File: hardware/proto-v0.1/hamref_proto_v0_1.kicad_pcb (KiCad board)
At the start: 4 copper layers, 100 x 100 mm, 113 parts, among them J1 5V_EXT, J10 J RUN (short=MCU reset), J11 J SPARE GPIO, J2 SMA ANT, J3 BNC REF OUT, J4 BNC 1PPS OUT, J5 BNC AUX OUT, J6 J OLED 0.91in I2C, J7 J ENCODER, J8 J LEDS (2x WS2812B), J9 J RESET GNSS (short=reset), U1 TPS2065C, U10 74AHCT1G125, U2 LP5907-3.3, U3 LEA-M8S-0, U4 74LVC1G17, U5 AD5693R, U6 74LVC1G17, U7 74AHCT1G125, U8 74LVC1G125, U9 Si5351C-B-GM, X1 OSC5A2B02, Y1 25MHz

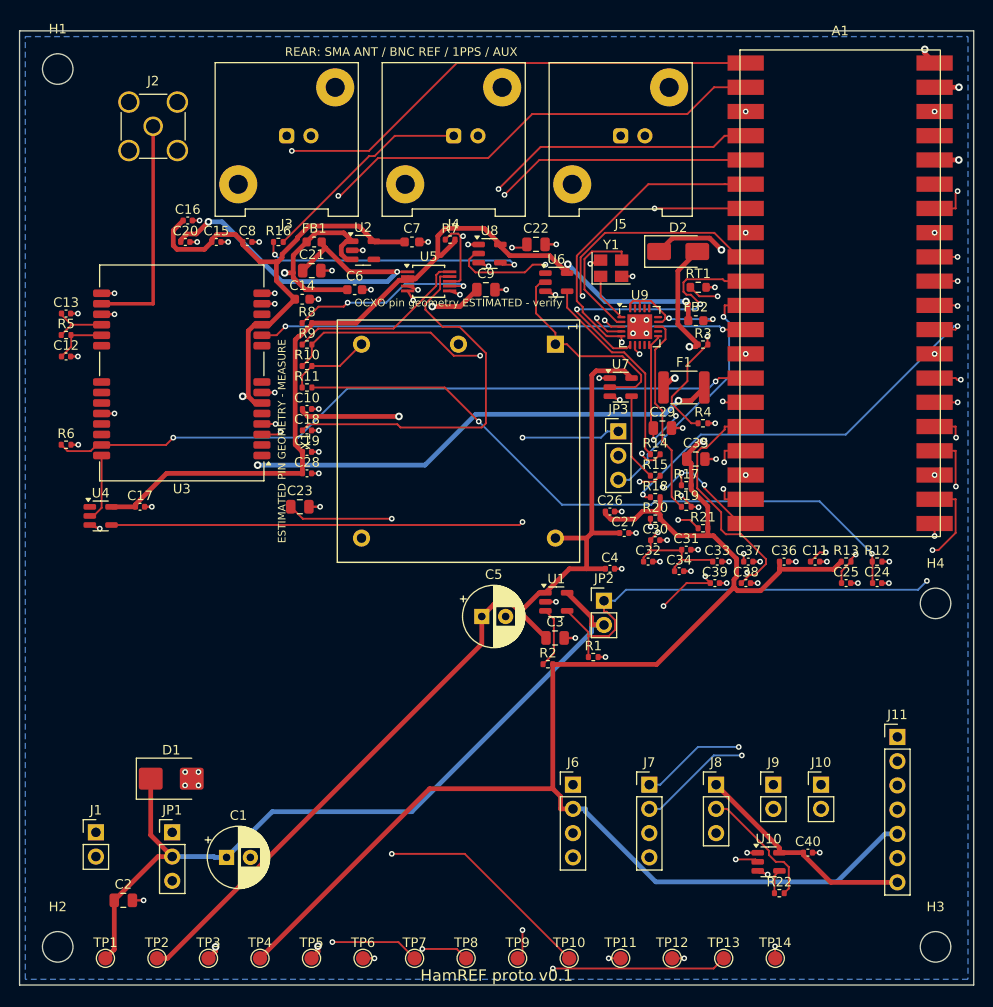
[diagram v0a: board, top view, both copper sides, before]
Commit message: Proto-PCB v0.1: logo, silk cleanup, 3D model paths
- Vectorised HamREF by OH2LAK logo + satellite from the enclosure mockup (make_logo.py)
- silk_pass.py: place reference designators after routing, avoiding pads/vias/outlines
- Fix 3D model paths for KiCad 10 (${KICAD10_3DMODEL_DIR}, .step); box models for OCXO and RP2350-Plus
- route.sh: resume Freerouting from previous partial result; run silk pass before DRC
- DRC: 0 unconnected, 0 clearance, no silk overlaps

Co-Authored-By: Claude Sonnet 5.5 <noreply@anthropic.com>
Claude-Session: https://claude.ai/code/session_01BBEBh5Nhxyv6s49uSZkpLo
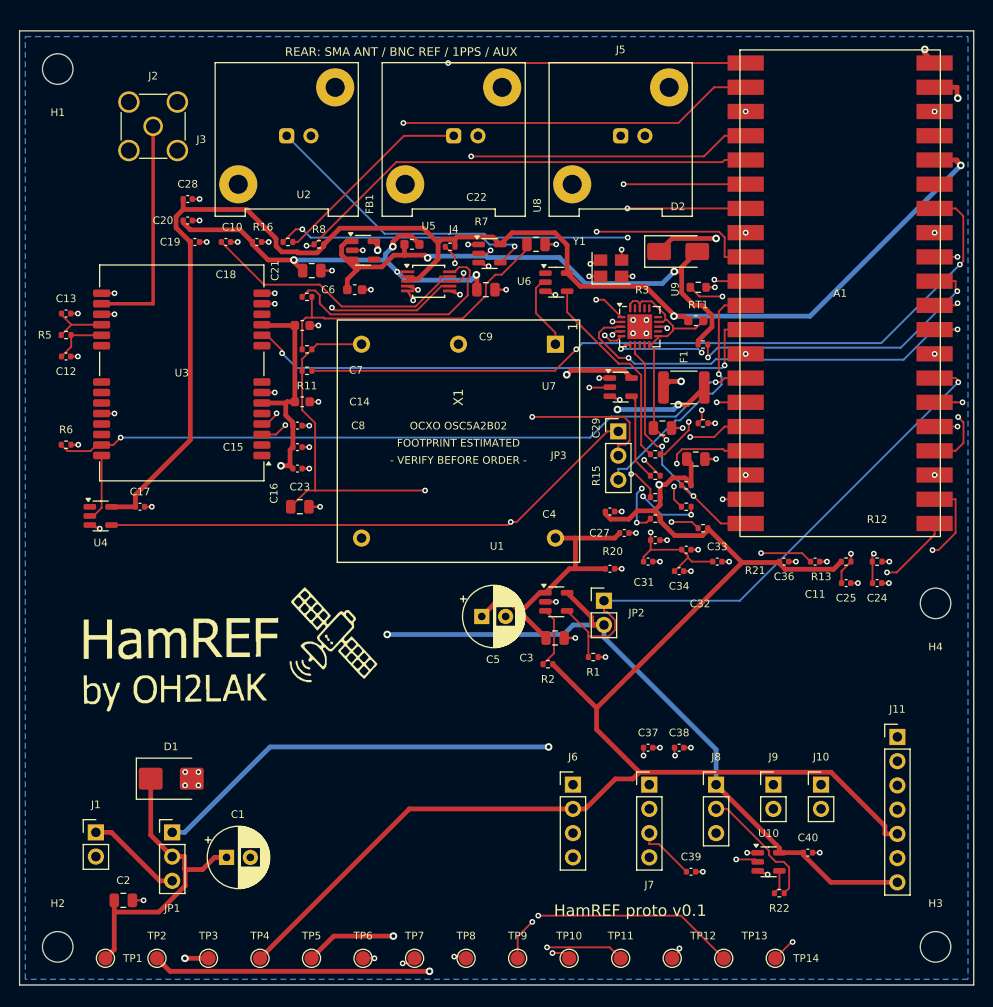
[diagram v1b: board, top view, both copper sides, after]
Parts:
- moved C28 31.3 mm to (67.6, 57.6)
- moved C39 30.4 mm to (120.4, 128.1)
- moved C16 28.4 mm to (79.1, 85.9)
- moved C19 24.9 mm to (68.4, 62.1)
- moved C15 23.1 mm to (79.1, 83.6)
- moved C37 22.1 mm to (115.9, 115.1)
- moved C18 21.5 mm to (71.6, 62.1)
- moved C8 20.0 mm to (79.1, 81.4)
- moved C38 18.6 mm to (119.1, 115.1)
- moved C10 18.3 mm to (74.9, 62.1)
- moved C7 14.5 mm to (79.6, 70.9)
- moved C14 10.8 mm to (79.6, 78.9)
- moved FB1 10.3 mm to (91.1, 62.4)
- moved R8 8.34 mm to (81.4, 62.4)
- moved R9 5.00 mm to (80.1, 67.9)
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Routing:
- net OCXO_10M_3V3: track 63.1 -> 34.1 mm, vias 3 -> 4
- net 5V_MAIN: track 262.7 -> 239.4 mm, vias 2 -> 3
- net 5V_OCXO: track 101.5 -> 123.2 mm, vias 0 -> 2
- net ADC_5V: track 86.3 -> 66.0 mm, vias 3 -> 4
- net ADC_NTC: track 79.9 -> 61.8 mm
- net GNSS_RXD: track 156.5 -> 174.2 mm
- net GNSS_TXD: track 144.5 -> 159.8 mm
- net I2C0_SDA: track 95.1 -> 110.2 mm, vias 2 -> 4
- net 3V3: track 309.0 -> 321.9 mm, vias 4 -> 3
- net 5V_DAC: track 135.9 -> 123.0 mm
- net I2C1_SCL: track 58.3 -> 70.8 mm, vias 3 -> 2
- net 3V3_SYN: track 61.3 -> 48.9 mm, vias 5 -> 2
- net DAC_VREF: track 40.5 -> 28.4 mm
- net PPS_GNSS: track 157.4 -> 146.1 mm, vias 4 -> 3
- net OCXO_EN: track 72.6 -> 61.9 mm, vias 2 -> 1
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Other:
- board text added: "- VERIFY BEFORE ORDER -"
- board text added: "FOOTPRINT ESTIMATED"
- board text added: "OCXO OSC5A2B02"
- board text removed: "OCXO pin geometry ESTIMATED - verify"

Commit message: Proto-PCB v0.1: silk labels for connectors, jumpers and test points
- silk_pass.py adds function and pin-name labels (J1, J6-J11, JP1-3), rear-panel names, TP net names
- Reference designators avoid tracks where possible
- Proto text moved under the logo

Co-Authored-By: Claude Sonnet 5.5 <noreply@anthropic.com>
Claude-Session: https://claude.ai/code/session_01BBEBh5Nhxyv6s49uSZkpLo
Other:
- board text added: "+5V"
- board text added: "1PPS"
- board text added: "3V3"
- board text added: "3V3_GN"
- board text added: "5V"
- board text added: "5V_DAC"
- board text added: "5V_OX"
- board text added: "A"
- board text added: "AUX"
- board text added: "B"
- board text added: "DIN"
- board text added: "EFC"
- board text added: "EN"
- board text added: "EN=short: OCXO always on"
- board text added: "ENCODER"
- board text added: "EXT 5V"
- board text added: "FLT"
- board text added: "GND"
- board text added: "GNSS ANT"
- board text added: "GNSS RST"
- board text added: "GP17"
- board text added: "GP18"
- board text added: "GP19"
- board text added: "GP20"
- board text added: "GRXD"
- board text added: "GTXD"
- board text added: "JP3 1PPS SRC 1-2 GNSS 2-3 MCU"
- board text added: "LEDS"
- board text added: "MCU RST"
- board text added: "OCXO"
- board text added: "OCXO ON"
- board text added: "OLED"
- board text added: "PPS"
- board text added: "PPS_G"
- board text added: "PWR SEL 1-2 USB 2-3 EXT"
- board text added: "REF 10M"
- board text added: "RUN"
- board text added: "SCL"
- board text added: "SDA"
- board text added: "SPARE"
- board text added: "SW"
- board text removed: "REAR: SMA ANT / BNC REF / 1PPS / AUX"

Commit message: Proto-PCB v0.1: GND pours on all copper planes, edge via fence, stitching vias
- F.Cu GND pour was missing (rule areas suppressed it in import_ses.py): fixed
- gnd_finish.py: thermal-relief pours, RF no-pour strip along GNSS_RF, edge via fence, 6 mm stitching grid
- route.sh: silk_pass then gnd_finish before DRC

Co-Authored-By: Claude Sonnet 5.5 <noreply@anthropic.com>
Claude-Session: https://claude.ai/code/session_01BBEBh5Nhxyv6s49uSZkpLo
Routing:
- net GND: vias 81 -> 259
- added copper zone on F.Cu, net GND

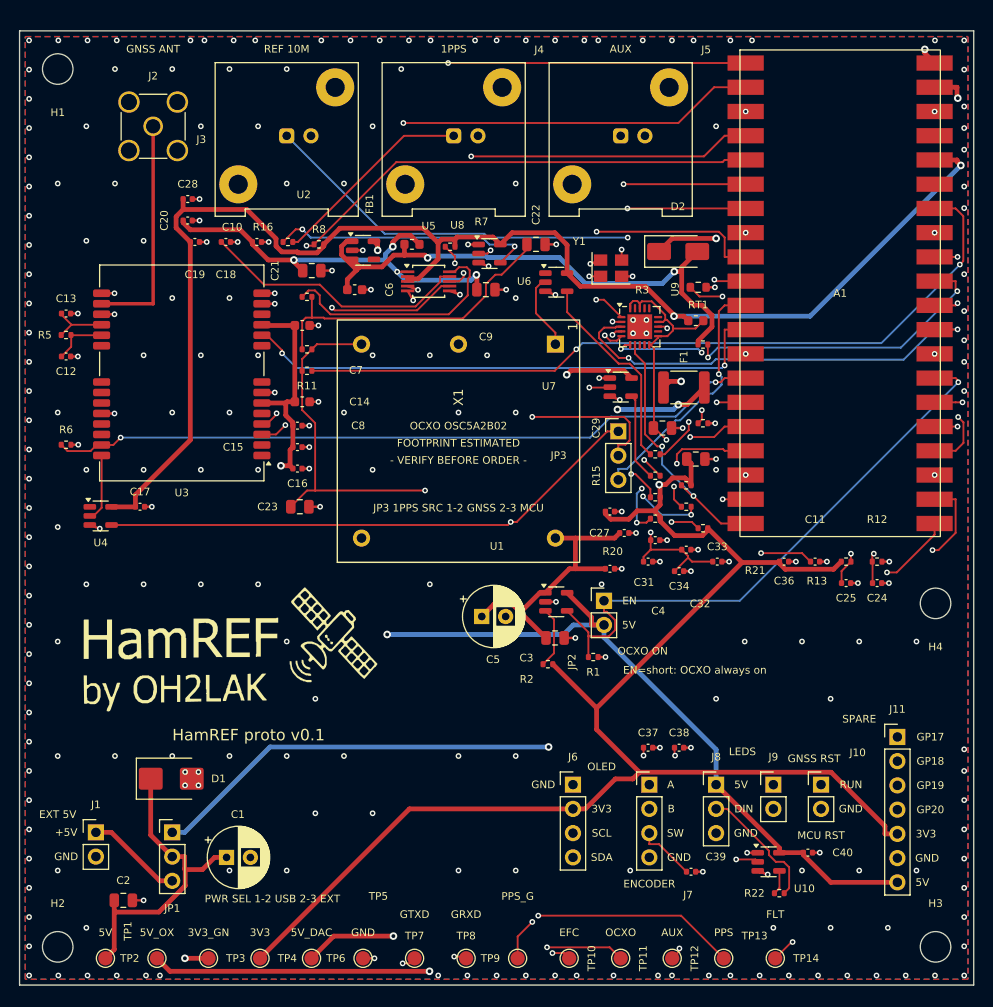
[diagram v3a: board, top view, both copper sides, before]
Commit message: Proto-PCB v0.1: fit Fischer AKG 105.26 case (100x80 mm)
Board 100x100 -> 100x80 mm, R1.5 mm corners, no mounting holes (slides into
case grooves), unmasked GND copper strips along both long edges, horizontal
BNC/SMA connectors for the 15.2 mm height budget, router/test-point fixes.
Docs updated to v0.18.

Co-Authored-By: Claude Sonnet 5.5 <noreply@anthropic.com>
Claude-Session: https://claude.ai/code/session_01BBEBh5Nhxyv6s49uSZkpLo
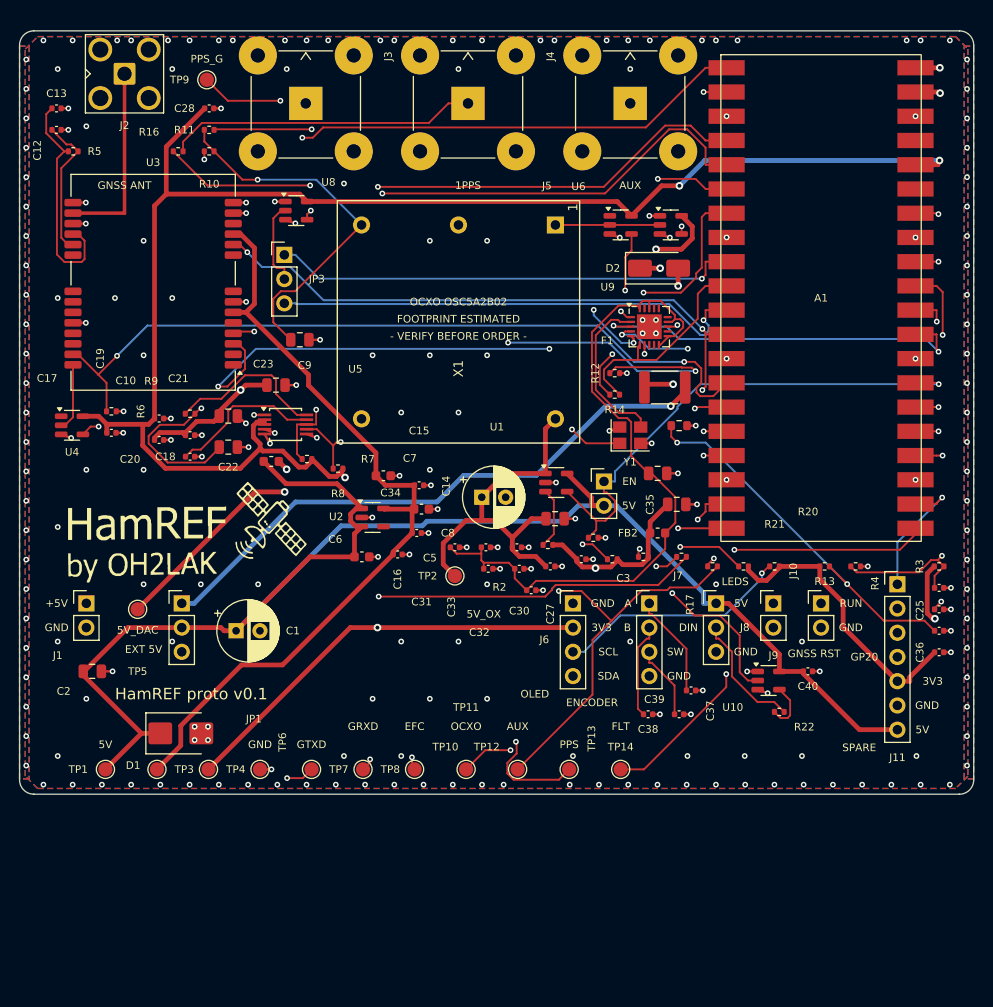
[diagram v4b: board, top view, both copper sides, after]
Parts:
- removed H1, H2, H3, H4: MountingHole_M3, MountingHole_3.2mm_M3
- J2: footprint SMA_Amphenol_901-144_Vertical -> SMA_Amphenol_901-143_Horizontal
- J3, J4, J5: footprint BNC_Amphenol_031-5539_Vertical -> BNC_TEConnectivity_1478035_Horizontal
- moved TP9 97.7 mm to (69.6, 45.1)
- moved TP2 50.8 mm to (95.6, 97.1)
- moved TP5 40.9 mm to (62.4, 100.6)
- moved JP3 39.6 mm to (77.8, 63.5)
- moved C22 38.6 mm to (71.9, 83.6)
- moved R3 34.0 mm to (146.4, 96.1)
- moved R12 33.9 mm to (112.4, 75.9)
- moved U2 28.0 mm to (87.0, 91.0)
- moved C6 28.0 mm to (85.9, 95.1)
- moved R11 27.3 mm to (69.9, 50.4)
- moved FB1 27.1 mm to (76.4, 85.1)
- moved R7 26.8 mm to (80.1, 84.9)
- moved TP11 25.6 mm to (96.8, 117.4)
- moved TP12 25.6 mm to (102.2, 117.4)
- moved TP13 25.6 mm to (107.6, 117.4)
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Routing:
- net 5V_DAC: track 123.0 -> 50.5 mm, vias 5 -> 4
- net 5V_OCXO: track 123.2 -> 68.3 mm, vias 2 -> 1
- net GNSS_RXD: track 174.2 -> 124.3 mm
- net PPS_GNSS: track 146.1 -> 108.4 mm
- net REF_BUF: track 9.16 -> 46.8 mm, vias 0 -> 2
- net GNSS_TXD: track 159.8 -> 126.4 mm, vias 3 -> 4
- net ADC_EFC: track 118.3 -> 150.7 mm, vias 3 -> 5
- net 5V_MAIN: track 239.4 -> 209.0 mm, vias 3 -> 2
- net 5V_USB: track 91.6 -> 62.4 mm, vias 3 -> 1
- net 3V3_GNSS: track 111.9 -> 85.1 mm, vias 3 -> 0
- net PPS_SEL: track 35.5 -> 8.91 mm, vias 2 -> 0
- net I2C1_SDA: track 47.3 -> 73.5 mm, vias 3 -> 2
- net 3V3_SYN: track 48.9 -> 74.2 mm, vias 2 -> 0
- net PPS_MCU: track 26.5 -> 50.7 mm
- net ENC_SW: track 56.2 -> 33.6 mm
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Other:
- board size 100 x 100 mm -> 100 x 80 mm
- board text removed: "3V3_GN"
- board text removed: "EN=short: OCXO always on"
- board text removed: "GP17"
- board text removed: "GP18"
- board text removed: "GP19"
- board text removed: "JP3 1PPS SRC 1-2 GNSS 2-3 MCU"
- board text removed: "MCU RST"
- board text removed: "OCXO ON"
- board text removed: "PWR SEL 1-2 USB 2-3 EXT"
- board text removed: "REF 10M"
